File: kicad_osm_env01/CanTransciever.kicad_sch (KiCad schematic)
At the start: 23 parts, among them U8 SN65HVD230

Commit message: assigned all footprints
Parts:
- C38: Voltage (none) -> 50V
- R25, R31, R38, R42, R43: footprint Resistor_SMD:R_0603_1608Metric -> Resistor_SMD:R_0402_1005Metric
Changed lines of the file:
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@@
   (title_block
     (title "Open Smart Monitor")
-    (date "2022-09-26")
-    (rev "C")
+    (date "2023-09-29")
+    (rev "C.2")
     (company "Devtank LTD")
     (comment 1 "Part No: 304-010")
@@
       (effects (font (size 1.27 1.27)) hide)
     )
+    (property "Voltage" "50V" (at 143.51 76.2 0)
+      (effects (font (size 1.27 1.27)) hide)
+    )
     (pin "1")
     (pin "2")
@@
       (effects (font (size 1.27 1.27)))
     )
-    (property "Footprint" "Resistor_SMD:R_0603_1608Metric" (at 156.718 76.2 90)
+    (property "Footprint" "Resistor_SMD:R_0402_1005Metric" (at 156.718 76.2 90)
       (effects (font (size 1.27 1.27)) hide)
     )
@@
       (effects (font (size 1.27 1.27)))
     )
-    (property "Footprint" "Resistor_SMD:R_0603_1608Metric" (at 111.125 99.822 90)
+    (property "Footprint" "Resistor_SMD:R_0402_1005Metric" (at 111.125 99.822 90)
       (effects (font (size 1.27 1.27)) hide)
     )
@@
       (effects (font (size 1.27 1.27)) (justify left))
     )
-    (property "Footprint" "Resistor_SMD:R_0603_1608Metric" (at 173.482 96.52 90)
+    (property "Footprint" "Resistor_SMD:R_0402_1005Metric" (at 173.482 96.52 90)
       (effects (font (size 1.27 1.27)) hide)
     )
@@
       (effects (font (size 1.27 1.27)))
     )
-    (property "Footprint" "Resistor_SMD:R_0603_1608Metric" (at 105.41 69.723 90)
+    (property "Footprint" "Resistor_SMD:R_0402_1005Metric" (at 105.41 69.723 90)
       (effects (font (size 1.27 1.27)) hide)
     )
@@
       (effects (font (size 1.27 1.27)))
     )
-    (property "Footprint" "Resistor_SMD:R_0603_1608Metric" (at 105.41 74.168 90)
-      (effects (font (size 1.27 1.27)) hide)
-    )
+    (property "Footprint" "Resistor_SMD:R_0402_1005Metric" (at 105.41 74.168 90)
+      (effects (font (size 1.27 1.27)) hide)
+    )

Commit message: added tracking to layout
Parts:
- TP22, TP23, TP41, TP80, TP81: footprint TestPoint:TestPoint_THTPad_D1.0mm_Drill0.5mm -> TestPoint:TestPoint_Pad_D1.5mm
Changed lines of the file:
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@@
     )
   )
-  (symbol (lib_id "Device:R") (at 175.26 106.045 0) (unit 1)
-    (in_bom yes) (on_board yes) (dnp no)
-    (property "Reference" "R87" (at 177.038 104.8766 0)
-      (effects (font (size 1.27 1.27)) (justify left))
-    )
-    (property "Value" "120R" (at 177.038 107.188 0)
-      (effects (font (size 1.27 1.27)) (justify left))
-    )
-    (property "Footprint" "Resistor_SMD:R_0603_1608Metric" (at 173.482 106.045 90)
+  (symbol (lib_id "Device:R") (at 175.26 106.045 0) (mirror y) (unit 1)
+    (in_bom yes) (on_board yes) (dnp no)
+    (property "Reference" "R87" (at 173.482 104.8766 0)
+      (effects (font (size 1.27 1.27)) (justify left))
+    )
+    (property "Value" "120R" (at 173.482 107.188 0)
+      (effects (font (size 1.27 1.27)) (justify left))
+    )
+    (property "Footprint" "Resistor_SMD:R_0603_1608Metric" (at 177.038 106.045 90)
       (effects (font (size 1.27 1.27)) hide)
     )
@@
       (effects (font (size 1.27 1.27)) hide)
     )
-    (property "Footprint" "TestPoint:TestPoint_THTPad_D1.0mm_Drill0.5mm" (at 111.76 88.265 0)
+    (property "Footprint" "TestPoint:TestPoint_Pad_D1.5mm" (at 111.76 88.265 0)
       (effects (font (size 1.27 1.27)) hide)
     )
@@
       (effects (font (size 1.27 1.27)) hide)
     )
-    (property "Footprint" "TestPoint:TestPoint_THTPad_D1.0mm_Drill0.5mm" (at 117.475 122.555 0)
+    (property "Footprint" "TestPoint:TestPoint_Pad_D1.5mm" (at 117.475 122.555 0)
       (effects (font (size 1.27 1.27)) hide)
     )
@@
       (effects (font (size 1.27 1.27)) hide)
     )
-    (property "Footprint" "TestPoint:TestPoint_THTPad_D1.0mm_Drill0.5mm" (at 109.22 100.965 0)
+    (property "Footprint" "TestPoint:TestPoint_Pad_D1.5mm" (at 109.22 100.965 0)
       (effects (font (size 1.27 1.27)) hide)
     )
@@
       (effects (font (size 1.27 1.27)) hide)
     )
-    (property "Footprint" "TestPoint:TestPoint_THTPad_D1.0mm_Drill0.5mm" (at 206.375 93.98 0)
+    (property "Footprint" "TestPoint:TestPoint_Pad_D1.5mm" (at 206.375 93.98 0)
       (effects (font (size 1.27 1.27)) hide)
     )
@@
       (effects (font (size 1.27 1.27)) hide)
     )
-    (property "Footprint" "TestPoint:TestPoint_THTPad_D1.0mm_Drill0.5mm" (at 206.375 118.11 0)
-      (effects (font (size 1.27 1.27)) hide)
-    )
+    (property "Footprint" "TestPoint:TestPoint_Pad_D1.5mm" (at 206.375 118.11 0)
+      (effects (font (size 1.27 1.27)) hide)
+    )

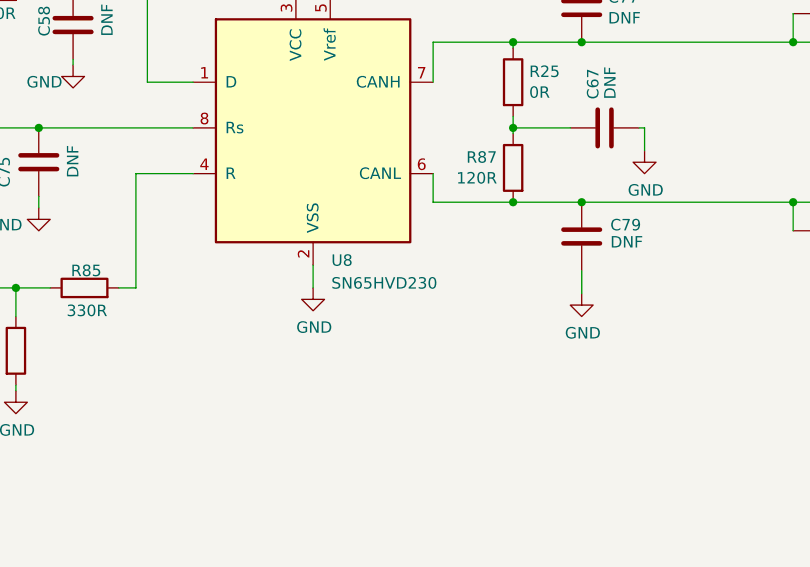
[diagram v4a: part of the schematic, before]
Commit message: added information to symbol entries table, added jumper settings table, minor single track update on layout
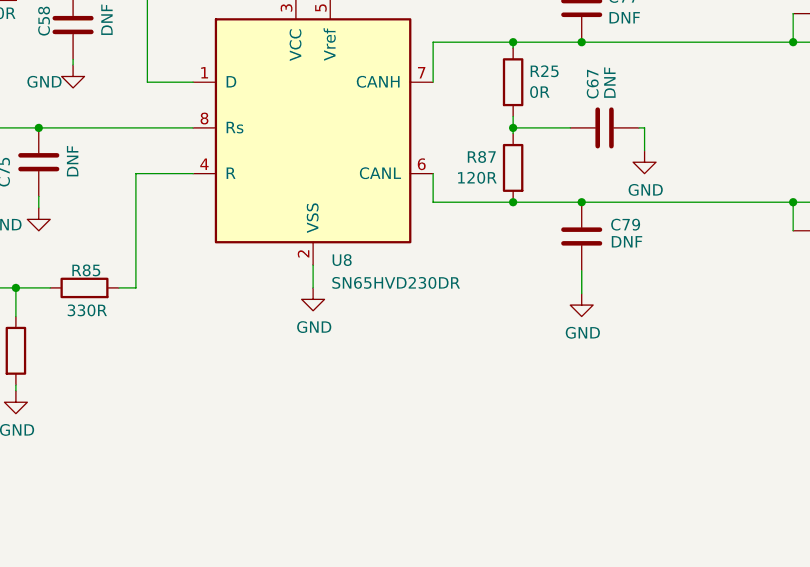
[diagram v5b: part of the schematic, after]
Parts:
- C37: Characteristics (none) -> X5R; Other (none) -> Can use own part, but needs to meet the specs; Voltage (none) -> 10V
- C38: Characteristics (none) -> X5R; Other (none) -> Can use own part, but needs to meet the specs
- C58, C67, C75, C77, C79: Characteristics (none) -> X5R; Voltage (none) -> 50V
- L6: Manufacturer (none) -> TDK; Manufacturer Part Number (none) -> MPZ1005S121HT000; Other (none) -> Can use own part, but needs to meet the specs
- R25, R31, R38, R42, R43, R83, R84, R85, R87: Tolerance (none) -> 1%
- U8: value SN65HVD230 -> SN65HVD230DR; Manufacturer (none) -> Texas Instruments; Manufacturer Part Number (none) -> SN65HVD230DR

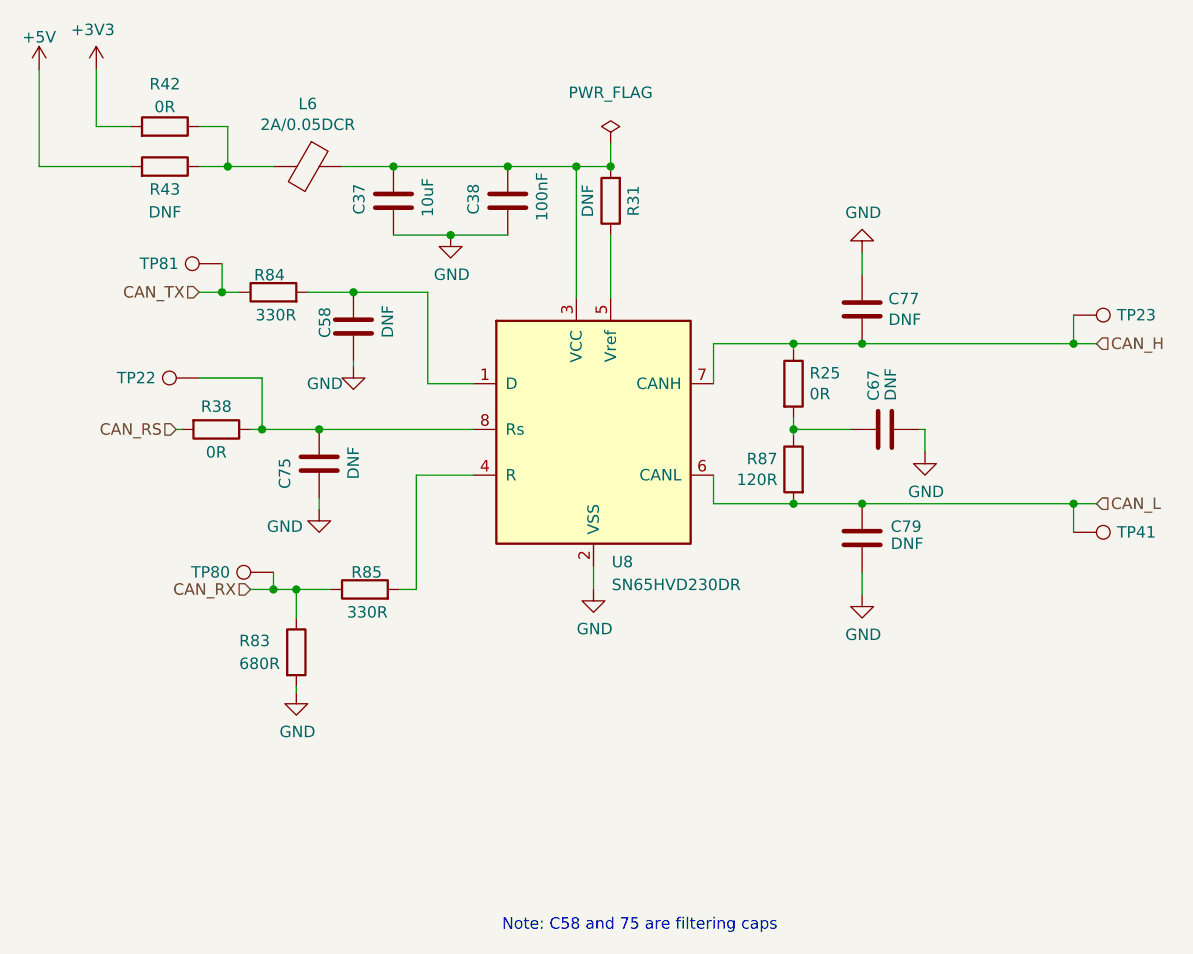
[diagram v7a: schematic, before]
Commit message: removed 0R links and DNF parts on schematics
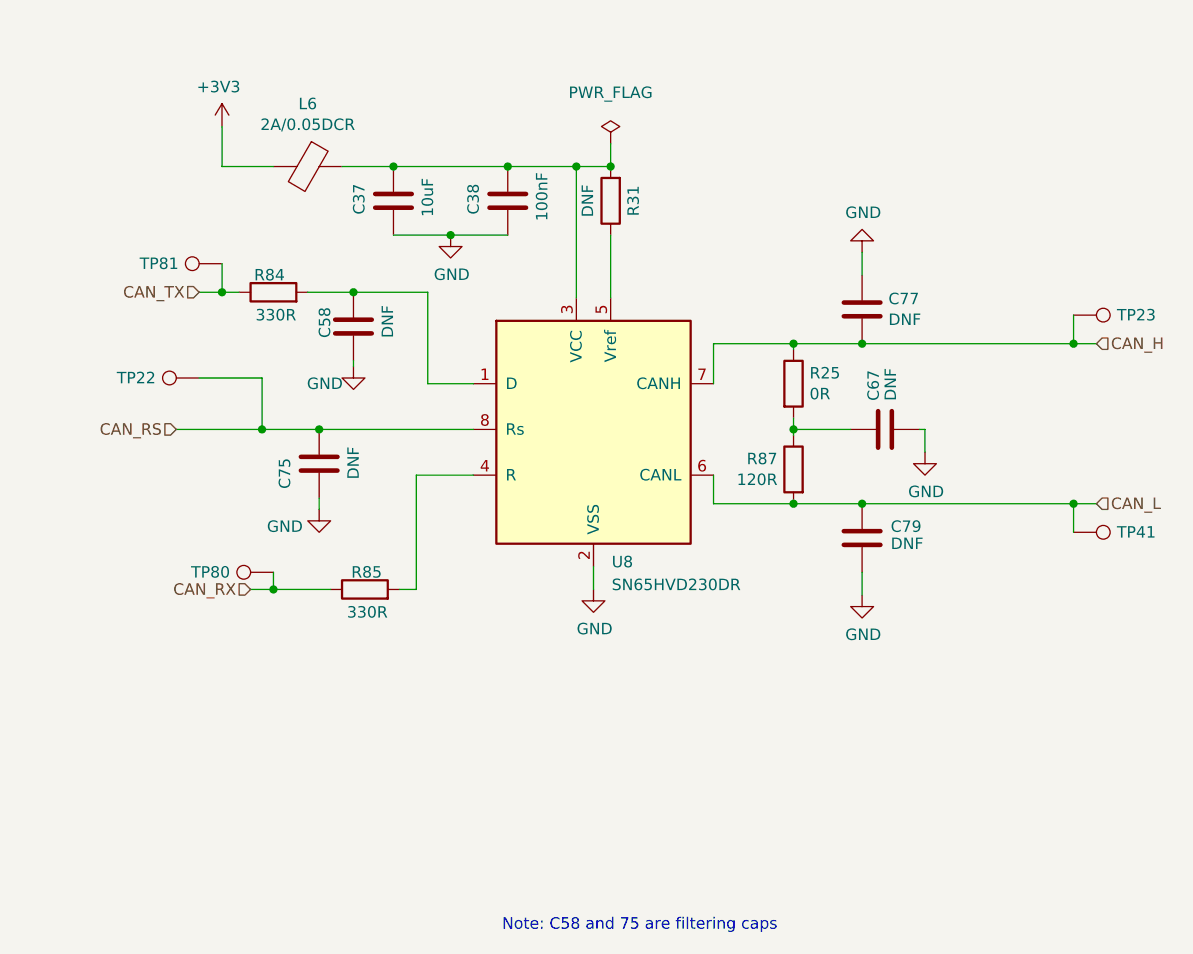
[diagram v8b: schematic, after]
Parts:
- removed R38, R42: 0R, Resistor_SMD:R_0402_1005Metric, symbol Device:R
- removed R43: DNF, Resistor_SMD:R_0402_1005Metric, symbol Device:R
- removed R83: 680R, Resistor_SMD:R_0603_1608Metric, symbol Device:R
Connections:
- net +3V3: now also L6.2
- net CAN_RS: now also C75.2, TP22.1, U8.8 (Rs)
